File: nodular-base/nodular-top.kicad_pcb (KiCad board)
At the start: 2 copper layers, 83.1 x 92.5 mm, 24 parts, among them SW1 SW_Push, SW2 SW_Push, SW3 SW_Push, SW4 SW_Push, SW5 SW_Push, SW6 SW_Push

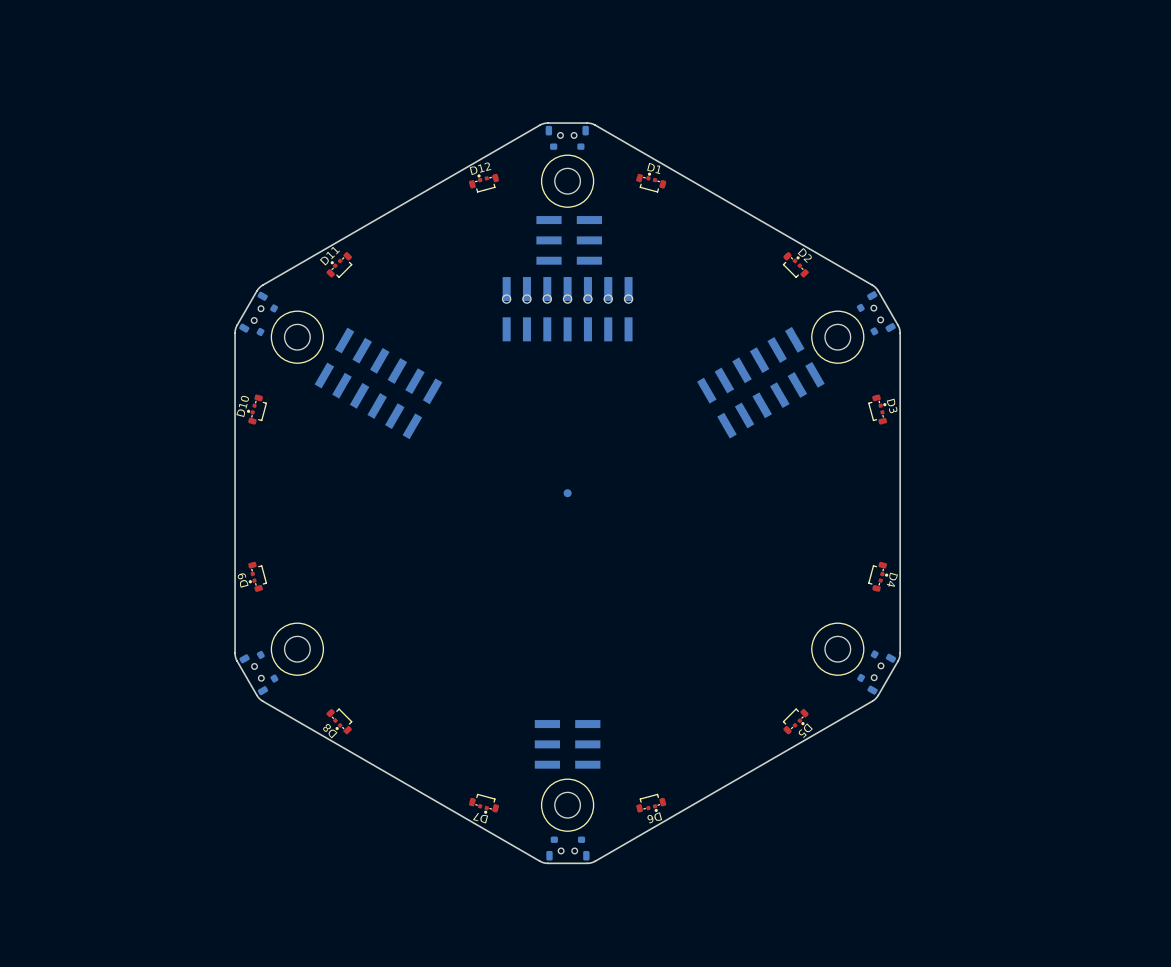
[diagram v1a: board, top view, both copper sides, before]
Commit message: Update layout for top board, add library items
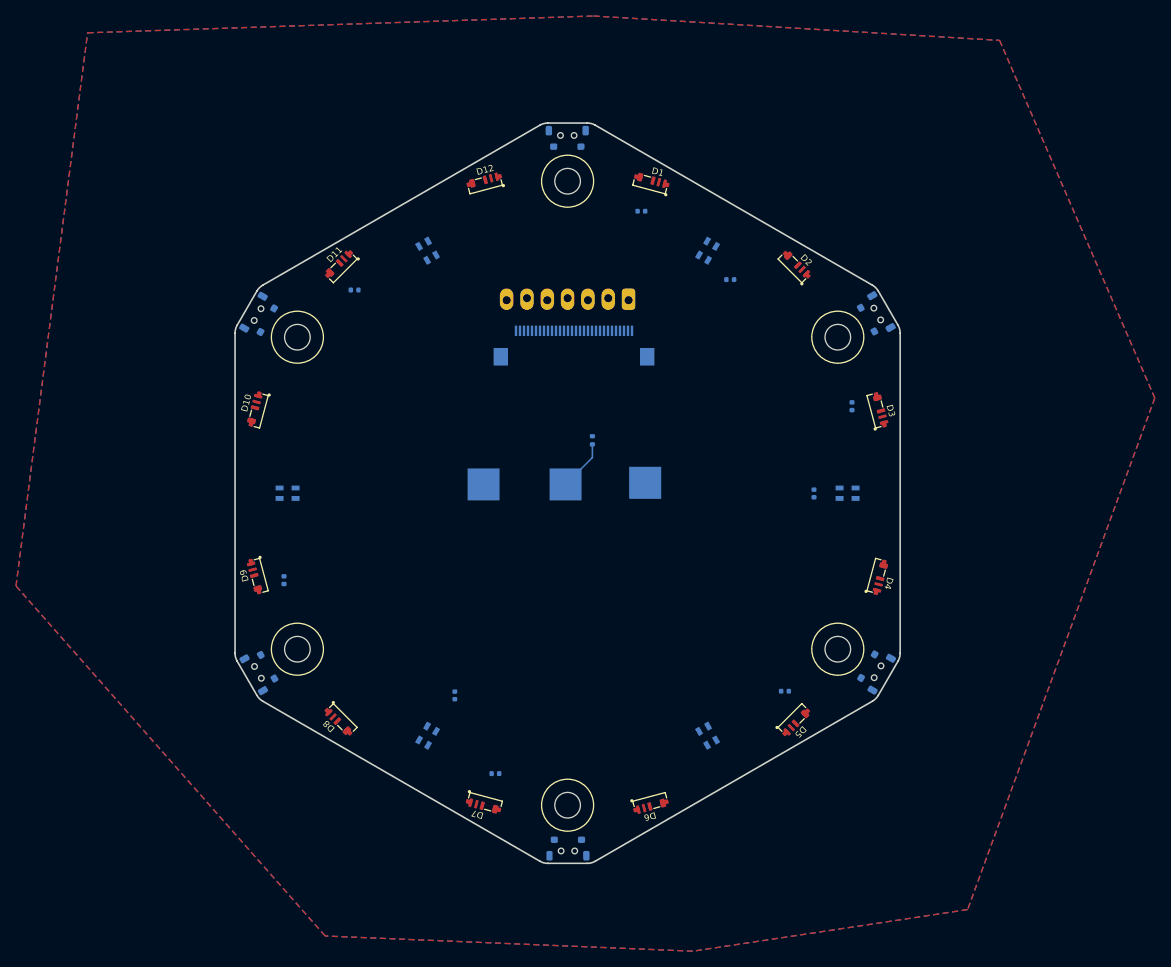
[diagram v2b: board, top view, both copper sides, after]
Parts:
- removed REF** (x2): PinHeader_2x03_P2.54mm_Vertical_SMD, Connector_PinHeader_2.54mm:PinHeader_2x03_P2.54mm_Vertical_SMD
- removed REF**: PinSocket_2x07_P2.54mm_Vertical_SMD, Connector_PinSocket_2.54mm:PinSocket_2x07_P2.54mm_Vertical_SMD
- removed REF** (x2): PinHeader_2x06_P2.54mm_Vertical_SMD, Connector_PinHeader_2.54mm:PinHeader_2x06_P2.54mm_Vertical_SMD
- removed REF**: TestPoint_Pad_D1.0mm, TestPoint:TestPoint_Pad_D1.0mm
- added C1: 1u, Capacitor_SMD:C_0402_1005Metric, B.Cu at (109.2, 64.8)
- added C2: 1u, Capacitor_SMD:C_0402_1005Metric, B.Cu at (135.6, 89.1)
- added C3: 1u, Capacitor_SMD:C_0402_1005Metric, B.Cu at (127.2, 124.8)
- added C4: 1u, Capacitor_SMD:C_0402_1005Metric, B.Cu at (91.0, 135.1)
- added C5: 1u, Capacitor_SMD:C_0402_1005Metric, B.Cu at (64.5, 110.9)
- added C6: 1u, Capacitor_SMD:C_0402_1005Metric, B.Cu at (73.4, 74.6)
- added C7: 1u, Capacitor_SMD:C_0402_1005Metric, B.Cu at (120.3, 73.3)
- added C8: 1u, Capacitor_SMD:C_0402_1005Metric, B.Cu at (85.9, 125.3)
- added C9: 1u, Capacitor_SMD:C_0402_1005Metric, B.Cu at (130.8, 100.0)
- added D13: SK6805MICRO-J, LED_SMD:LED_SK6805_PLCC4_2.4x2.7mm_P1.3mm, B.Cu at (117.5, 69.7)
- added D14: SK6805MICRO-J, LED_SMD:LED_SK6805_PLCC4_2.4x2.7mm_P1.3mm, B.Cu at (135.0, 100.0)
- added D15: SK6805MICRO-J, LED_SMD:LED_SK6805_PLCC4_2.4x2.7mm_P1.3mm, B.Cu at (117.5, 130.3)
- added D16: SK6805MICRO-J, LED_SMD:LED_SK6805_PLCC4_2.4x2.7mm_P1.3mm, B.Cu at (82.5, 130.3)
- added D17: SK6805MICRO-J, LED_SMD:LED_SK6805_PLCC4_2.4x2.7mm_P1.3mm, B.Cu at (65.0, 100.0)
- added D18: SK6805MICRO-J, LED_SMD:LED_SK6805_PLCC4_2.4x2.7mm_P1.3mm, B.Cu at (82.5, 69.7)
- added J1: Conn_01x30_MountingPin, Connector_FFC-FPC:Hirose_FH12-30S-0.5SH_1x30-1MP_P0.50mm_Horizontal, B.Cu at (100.8, 81.5)
- added R1: 1k, Resistor_SMD:R_0402_1005Metric, B.Cu at (103.1, 93.4)
- added TP1: TestPoint, TestPoint:TestPoint_Pad_4.0x4.0mm, B.Cu at (89.5, 98.9)
- added TP2: TestPoint, TestPoint:TestPoint_Pad_4.0x4.0mm, B.Cu at (99.8, 98.9)
- added TP3: TestPoint, TestPoint:TestPoint_Pad_4.0x4.0mm, B.Cu at (109.7, 98.7)
- added U1: ~, nodular:PinHeader_1x07_P2.54mm_Vertical_LockPads, B.Cu at (100.0, 75.8)
- D1, D10, D11, D12, D2, D3, D4, D5, D6, D7, D8, D9: footprint nodular:SK68XX-EC3210F -> nodular:SK6805SIDE-S
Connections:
- D1 pad 1: GND -> /LED/LED_POWER
- D1 pad 2: Net-(D1-DOUT) -> GND
- D1 pad 3: unconnected-(D1-DIN-Pad3) -> Net-(D1-DOUT)
- D1 pad 4: Net-(D1-VDD) -> Net-(D1-DIN)
- D10 pad 1: GND -> /LED/LED_POWER
- D10 pad 2: Net-(D10-DOUT) -> GND
- D10 pad 4: Net-(D1-VDD) -> Net-(D10-VDD)
- D11 pad 1: GND -> /LED/LED_POWER
- D11 pad 2: Net-(D11-DOUT) -> GND
- D11 pad 3: Net-(D10-DOUT) -> Net-(D11-DIN)
- D11 pad 4: Net-(D1-VDD) -> Net-(D10-DIN)
- D12 pad 1: GND -> /LED/LED_POWER
- D12 pad 2: unconnected-(D12-DOUT-Pad2) -> GND
- D12 pad 3: Net-(D11-DOUT) -> Net-(D12-DIN)
- D12 pad 4: Net-(D1-VDD) -> Net-(D11-DIN)
- D2 pad 1: GND -> /LED/LED_POWER
- D2 pad 2: Net-(D2-DOUT) -> GND
- D2 pad 3: Net-(D1-DOUT) -> Net-(D2-DIN)
- D2 pad 4: Net-(D1-VDD) -> Net-(D1-DOUT)
- D3 pad 1: GND -> /LED/LED_POWER
- D3 pad 2: Net-(D3-DOUT) -> GND
- D3 pad 3: Net-(D2-DOUT) -> Net-(D3-DIN)
- D3 pad 4: Net-(D1-VDD) -> Net-(D2-DIN)
- D4 pad 1: GND -> /LED/LED_POWER
- D4 pad 2: Net-(D4-DOUT) -> GND
- D4 pad 3: Net-(D3-DOUT) -> Net-(D4-DIN)
- D4 pad 4: Net-(D1-VDD) -> Net-(D3-DIN)
- D5 pad 1: GND -> /LED/LED_POWER
- D5 pad 2: Net-(D5-DOUT) -> GND
- D5 pad 3: Net-(D4-DOUT) -> Net-(D5-DIN)
- D5 pad 4: Net-(D1-VDD) -> Net-(D4-DIN)
- D6 pad 1: GND -> /LED/LED_POWER
- D6 pad 2: Net-(D6-DOUT) -> GND
- D6 pad 3: Net-(D5-DOUT) -> Net-(D6-DIN)
- D6 pad 4: Net-(D1-VDD) -> Net-(D5-DIN)
- D7 pad 1: GND -> /LED/LED_POWER
- D7 pad 2: Net-(D7-DOUT) -> GND
- D7 pad 3: Net-(D6-DOUT) -> Net-(D7-DIN)
- D7 pad 4: Net-(D1-VDD) -> Net-(D6-DIN)
- D8 pad 1: GND -> /LED/LED_POWER
- D8 pad 2: Net-(D8-DOUT) -> GND
- D8 pad 3: Net-(D7-DOUT) -> Net-(D8-DIN)
- D8 pad 4: Net-(D1-VDD) -> Net-(D7-DIN)
- D9 pad 1: GND -> /LED/LED_POWER
- D9 pad 2: Net-(D10-DIN) -> GND
- D9 pad 3: Net-(D8-DOUT) -> Net-(D10-VDD)
- D9 pad 4: Net-(D1-VDD) -> Net-(D8-DIN)
- SW1 pad 1: unconnected-(SW1-Pad1) -> /LED/SW1
- SW2 pad 1: unconnected-(SW2-Pad1) -> /LED/SW2
- SW3 pad 1: unconnected-(SW3-Pad1) -> /LED/SW3
- SW4 pad 1: unconnected-(SW4-Pad1) -> /LED/SW4
- SW5 pad 1: unconnected-(SW5-Pad1) -> /LED/SW5
- SW6 pad 1: unconnected-(SW6-Pad1) -> /LED/SW6
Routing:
- net /LED/LED_DATA: track 0.00 -> 6.39 mm
- added copper zone on B.Cu, net GND
- added copper zone on F.Cu, net GND
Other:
- board text added: "GND"
- board text added: "LED_DATA"
- board text added: "LED_PWR"

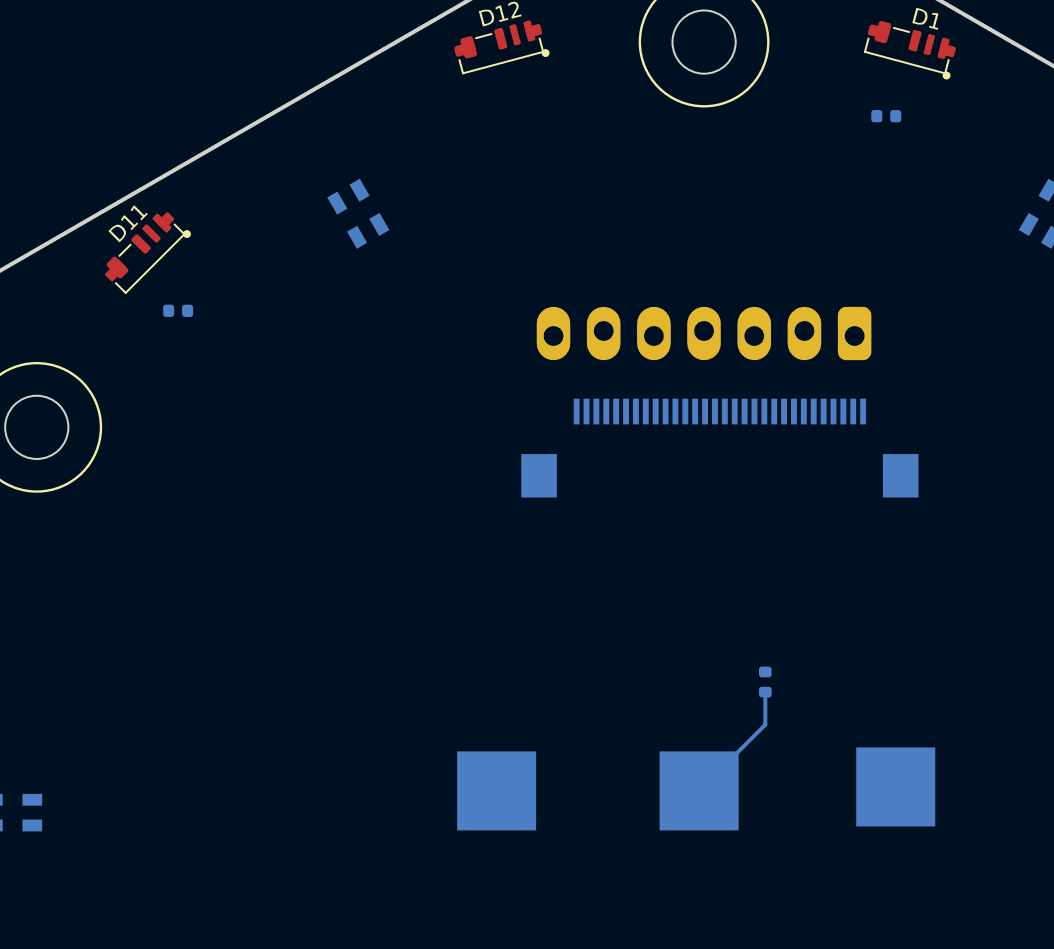
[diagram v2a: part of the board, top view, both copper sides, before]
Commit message: Add hole Add decoupling caps, pullups, and voltage dividers Set current limit on PMIC Determine battery attachment angle Update BOM and pinouts
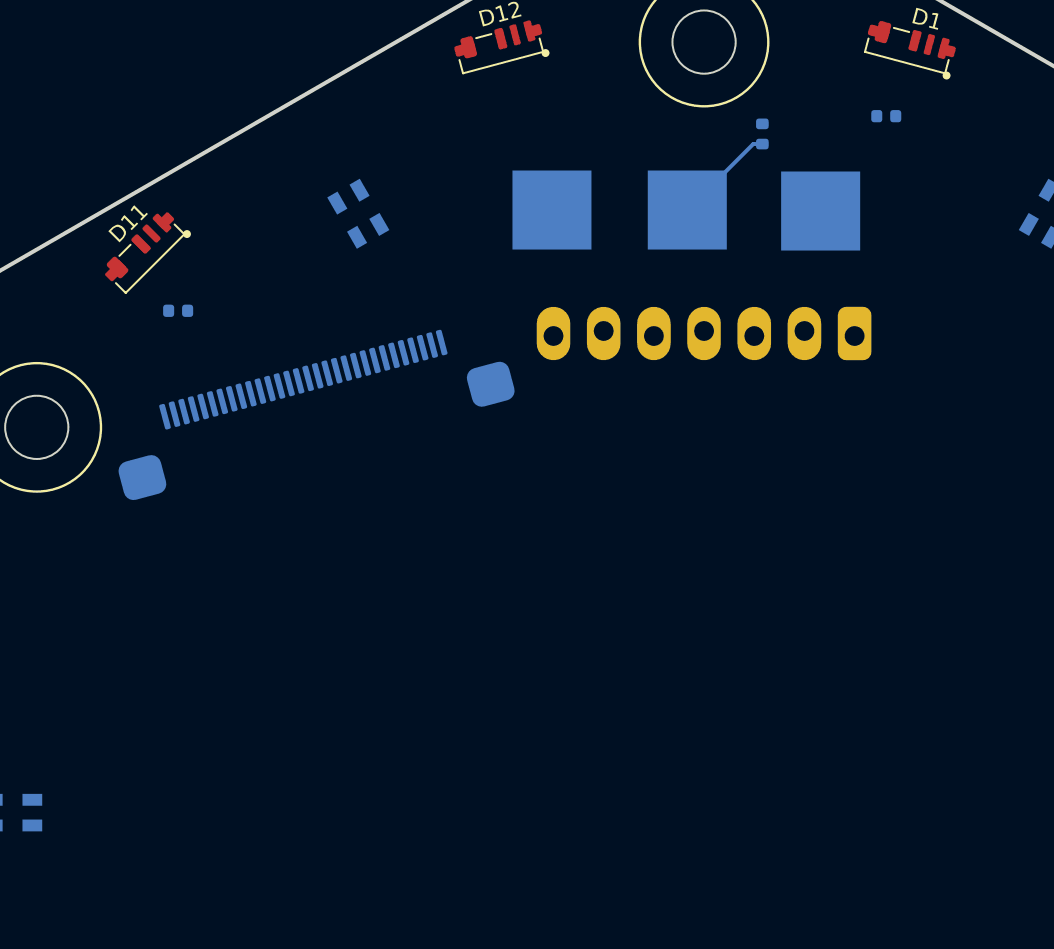
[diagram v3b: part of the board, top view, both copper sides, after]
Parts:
- J1: footprint Connector_FFC-FPC:Hirose_FH12-30S-0.5SH_1x30-1MP_P0.50mm_Horizontal -> nodular:Jushuo_AFC01-S30FCC-00_1x30-1MP_P0.50mm_Horizontal
- moved TP1 29.5 mm to (92.3, 69.5)
- moved TP2 29.4 mm to (99.2, 69.5)
- moved TP3 29.4 mm to (105.9, 69.5)
- moved R1 27.7 mm to (103.0, 65.7)
- moved J1 20.3 mm to (80.5, 81.1), turned to -165 degrees
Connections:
- C1 pad 1: /LED/LED_POWER -> /VBAT_SW
- C2 pad 1: /LED/LED_POWER -> /VBAT_SW
- C3 pad 1: /LED/LED_POWER -> /VBAT_SW
- C4 pad 1: /LED/LED_POWER -> /VBAT_SW
- C5 pad 1: /LED/LED_POWER -> /VBAT_SW
- C6 pad 1: /LED/LED_POWER -> /VBAT_SW
- C7 pad 1: /LED/LED_POWER -> /VBAT_SW
- C8 pad 1: /LED/LED_POWER -> /VBAT_SW
- C9 pad 1: /LED/LED_POWER -> /VBAT_SW
- D1 pad 1: /LED/LED_POWER -> /VBAT_SW
- D10 pad 1: /LED/LED_POWER -> /VBAT_SW
- D11 pad 1: /LED/LED_POWER -> /VBAT_SW
- D12 pad 1: /LED/LED_POWER -> /VBAT_SW
- D13 pad 4: /LED/LED_POWER -> /VBAT_SW
- D14 pad 4: /LED/LED_POWER -> /VBAT_SW
- D15 pad 4: /LED/LED_POWER -> /VBAT_SW
- D16 pad 4: /LED/LED_POWER -> /VBAT_SW
- D17 pad 4: /LED/LED_POWER -> /VBAT_SW
- D18 pad 4: /LED/LED_POWER -> /VBAT_SW
- D2 pad 1: /LED/LED_POWER -> /VBAT_SW
- D3 pad 1: /LED/LED_POWER -> /VBAT_SW
- D4 pad 1: /LED/LED_POWER -> /VBAT_SW
- D5 pad 1: /LED/LED_POWER -> /VBAT_SW
- D6 pad 1: /LED/LED_POWER -> /VBAT_SW
- D7 pad 1: /LED/LED_POWER -> /VBAT_SW
- D8 pad 1: /LED/LED_POWER -> /VBAT_SW
- D9 pad 1: /LED/LED_POWER -> /VBAT_SW
- J1 pad 1: unconnected-(J1-Pin_1-Pad1) -> GND
- J1 pad 10: unconnected-(J1-Pin_10-Pad10) -> /LS1
- J1 pad 11: unconnected-(J1-Pin_11-Pad11) -> GND
- J1 pad 12: unconnected-(J1-Pin_12-Pad12) -> /HS4
- J1 pad 13: unconnected-(J1-Pin_13-Pad13) -> /HS3
- J1 pad 14: unconnected-(J1-Pin_14-Pad14) -> /HS2
- J1 pad 15: unconnected-(J1-Pin_15-Pad15) -> /HS1
- J1 pad 16: unconnected-(J1-Pin_16-Pad16) -> GND
- J1 pad 17: unconnected-(J1-Pin_17-Pad17) -> GND
- J1 pad 18: unconnected-(J1-Pin_18-Pad18) -> /3V3
- J1 pad 19: unconnected-(J1-Pin_19-Pad19) -> /3V3
- J1 pad 2: unconnected-(J1-Pin_2-Pad2) -> GND
- J1 pad 20: unconnected-(J1-Pin_20-Pad20) -> /BTN6
- J1 pad 21: unconnected-(J1-Pin_21-Pad21) -> /BTN5
- J1 pad 22: unconnected-(J1-Pin_22-Pad22) -> /BTN4
- J1 pad 23: unconnected-(J1-Pin_23-Pad23) -> /BTN3
- J1 pad 24: unconnected-(J1-Pin_24-Pad24) -> /BTN2
- J1 pad 25: unconnected-(J1-Pin_25-Pad25) -> /BTN1
- J1 pad 26: unconnected-(J1-Pin_26-Pad26) -> GND
- J1 pad 27: unconnected-(J1-Pin_27-Pad27) -> /VBAT_SW
- J1 pad 28: unconnected-(J1-Pin_28-Pad28) -> /VBAT_SW
- J1 pad 29: unconnected-(J1-Pin_29-Pad29) -> /LED_DATA
- J1 pad 3: unconnected-(J1-Pin_3-Pad3) -> /ESPRX
- J1 pad 30: unconnected-(J1-Pin_30-Pad30) -> GND
- J1 pad 4: unconnected-(J1-Pin_4-Pad4) -> /ESPTX
- J1 pad 5: unconnected-(J1-Pin_5-Pad5) -> /ESPRESET
- J1 pad 6: unconnected-(J1-Pin_6-Pad6) -> /ESPBL
- J1 pad 7: unconnected-(J1-Pin_7-Pad7) -> /SCL
- J1 pad 8: unconnected-(J1-Pin_8-Pad8) -> /SDA
- J1 pad 9: unconnected-(J1-Pin_9-Pad9) -> /LS2
- J1 pad MP: unconnected-(J1-MountPin-PadMP) -> GND
- R1 pad 1: /LED/LED_DATA -> /LED_DATA
- SW1 pad 1: /LED/SW1 -> /BTN1
- SW2 pad 1: /LED/SW2 -> /BTN2
- SW3 pad 1: /LED/SW3 -> /BTN3
- SW4 pad 1: /LED/SW4 -> /BTN4
- SW5 pad 1: /LED/SW5 -> /BTN5
- SW6 pad 1: /LED/SW6 -> /BTN6
- TP1 pad 1: /LED/LED_POWER -> /VBAT_SW
- TP2 pad 1: /LED/LED_DATA -> /LED_DATA
- U1 pad 1: unconnected-(U1-RST-Pad1) -> /LS2
- U1 pad 2: unconnected-(U1-~{CS}-Pad2) -> /HS4
- U1 pad 3: unconnected-(U1-DC-Pad3) -> /HS3
- U1 pad 4: unconnected-(U1-SDI-Pad4) -> /HS2
- U1 pad 5: unconnected-(U1-CLK-Pad5) -> /HS1
- U1 pad 6: unconnected-(U1-GND-Pad6) -> GND
- U1 pad 7: unconnected-(U1-VCC-Pad7) -> /3V3
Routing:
- net /LED/LED_DATA: track 6.39 -> 0.00 mm
- net /LED_DATA: track 0.00 -> 5.18 mm
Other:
- board text added: "3V3"
- board text added: "CLK"
- board text added: "CS"
- board text added: "DC"
- board text added: "RESET"
- board text added: "SDI"

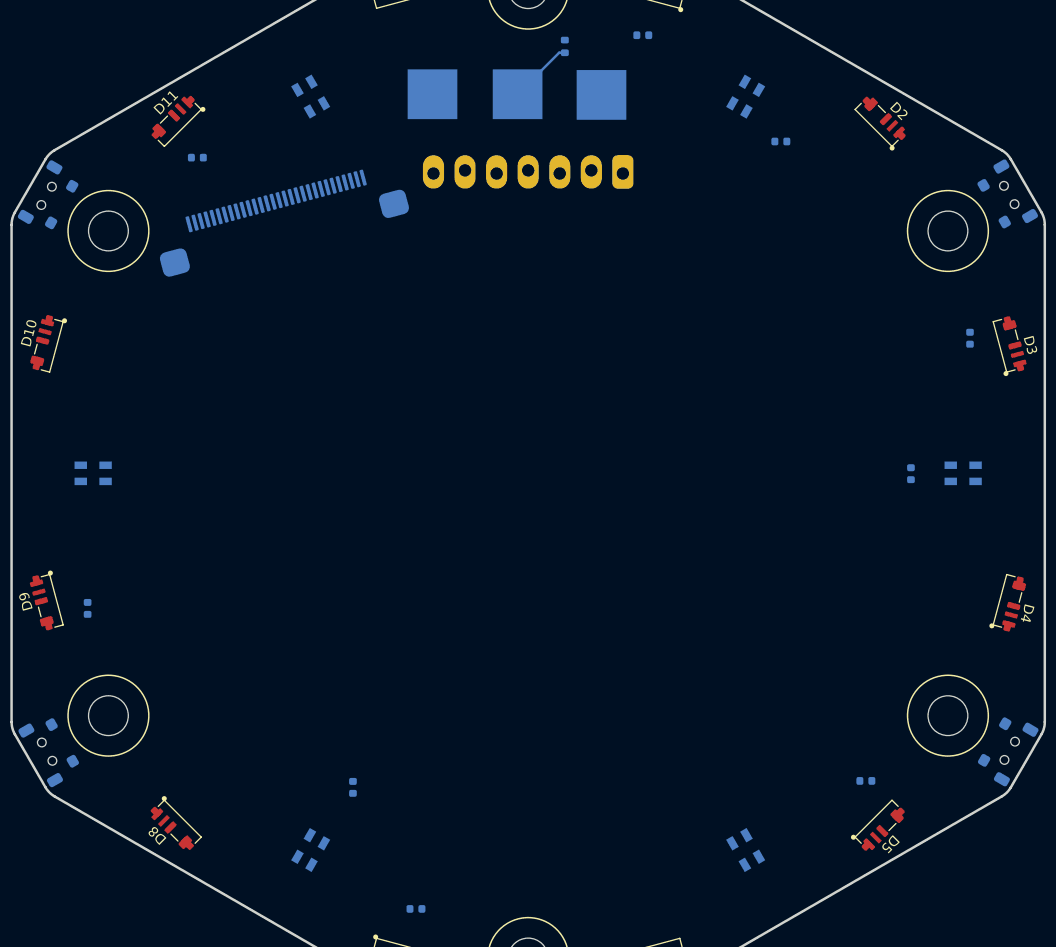
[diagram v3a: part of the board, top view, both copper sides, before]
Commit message: Add 3d models and fix erc errors
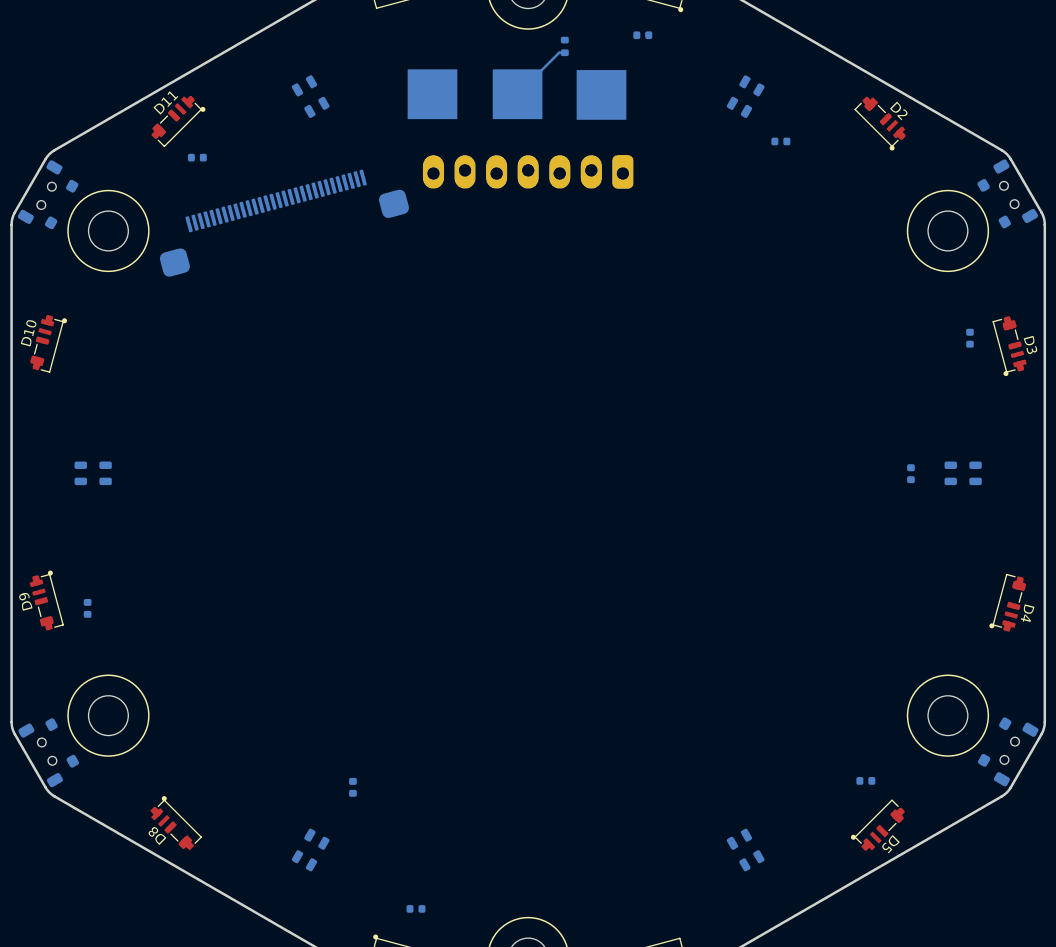
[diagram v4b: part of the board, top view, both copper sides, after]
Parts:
- D13, D14, D15, D16, D17, D18: footprint LED_SMD:LED_SK6805_PLCC4_2.4x2.7mm_P1.3mm -> nodular:LED_SK6805_PLCC4_2.4x2.7mm_P1.3mm
